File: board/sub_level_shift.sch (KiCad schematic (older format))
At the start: 24 parts, among them Q1401 Q_NPN_BEC, Q1402 Q_NPN_BEC, Q1403 Q_NPN_BEC, U1401 74LVC4245A, U1402 74LVC4245A, U1403 74LVC4245A, U1404 74LVC4245A, U1405 74LVC4245A, U1406 74LVC4245A, U1407 74LVC4245A

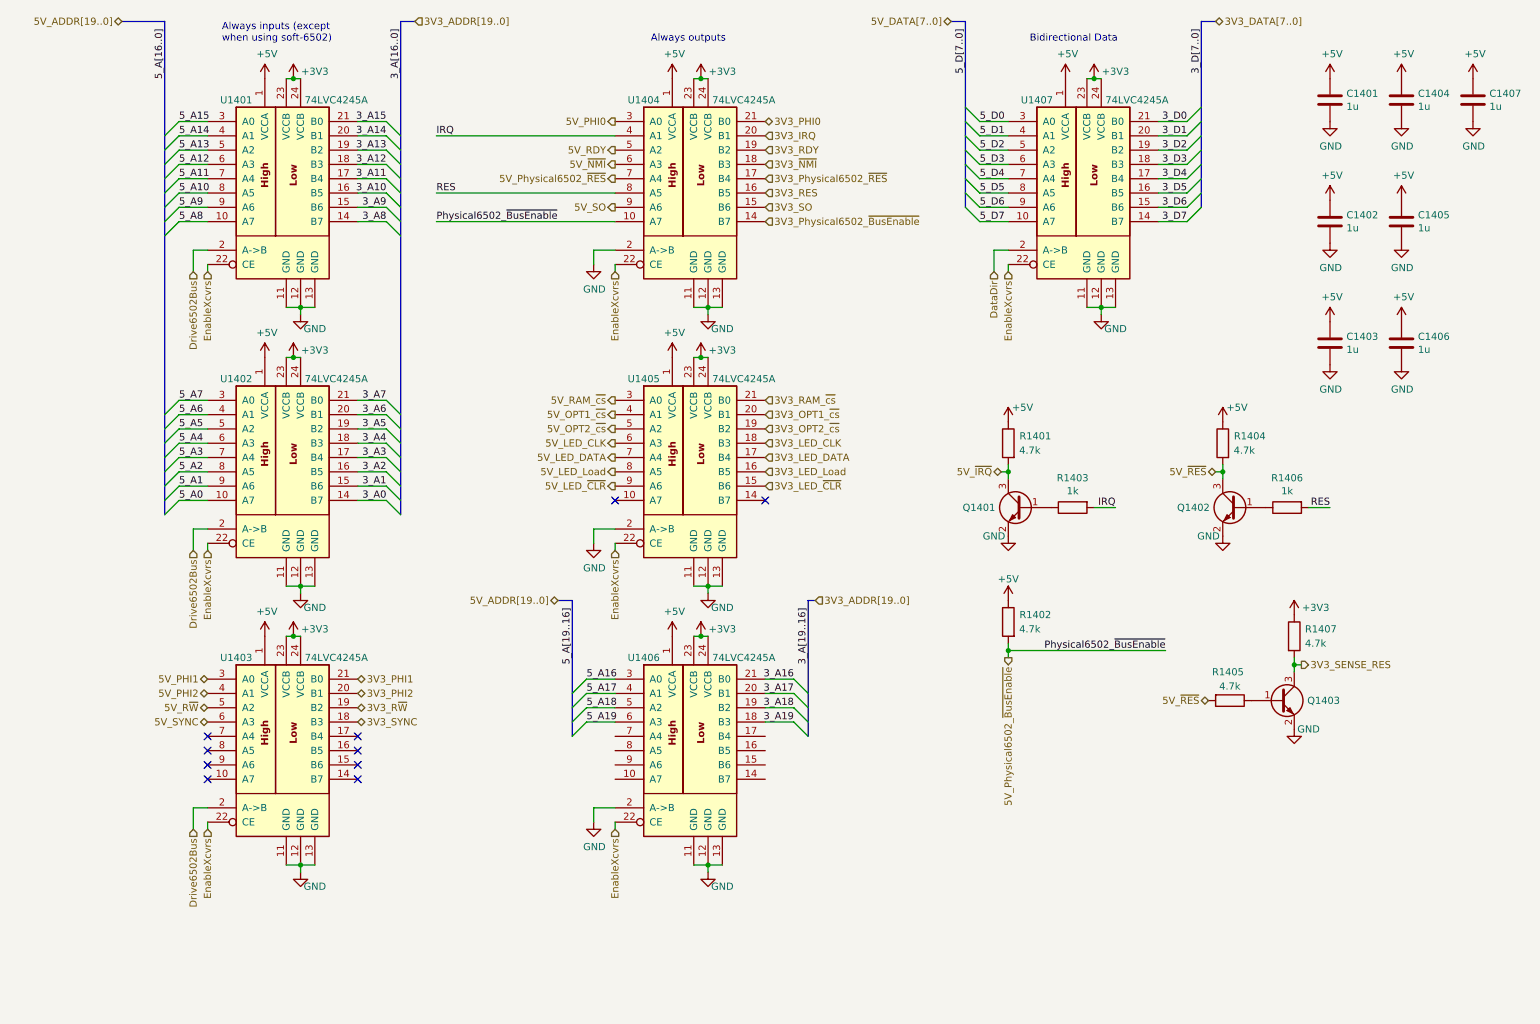
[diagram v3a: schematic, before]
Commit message: made some changes based on projected power budget
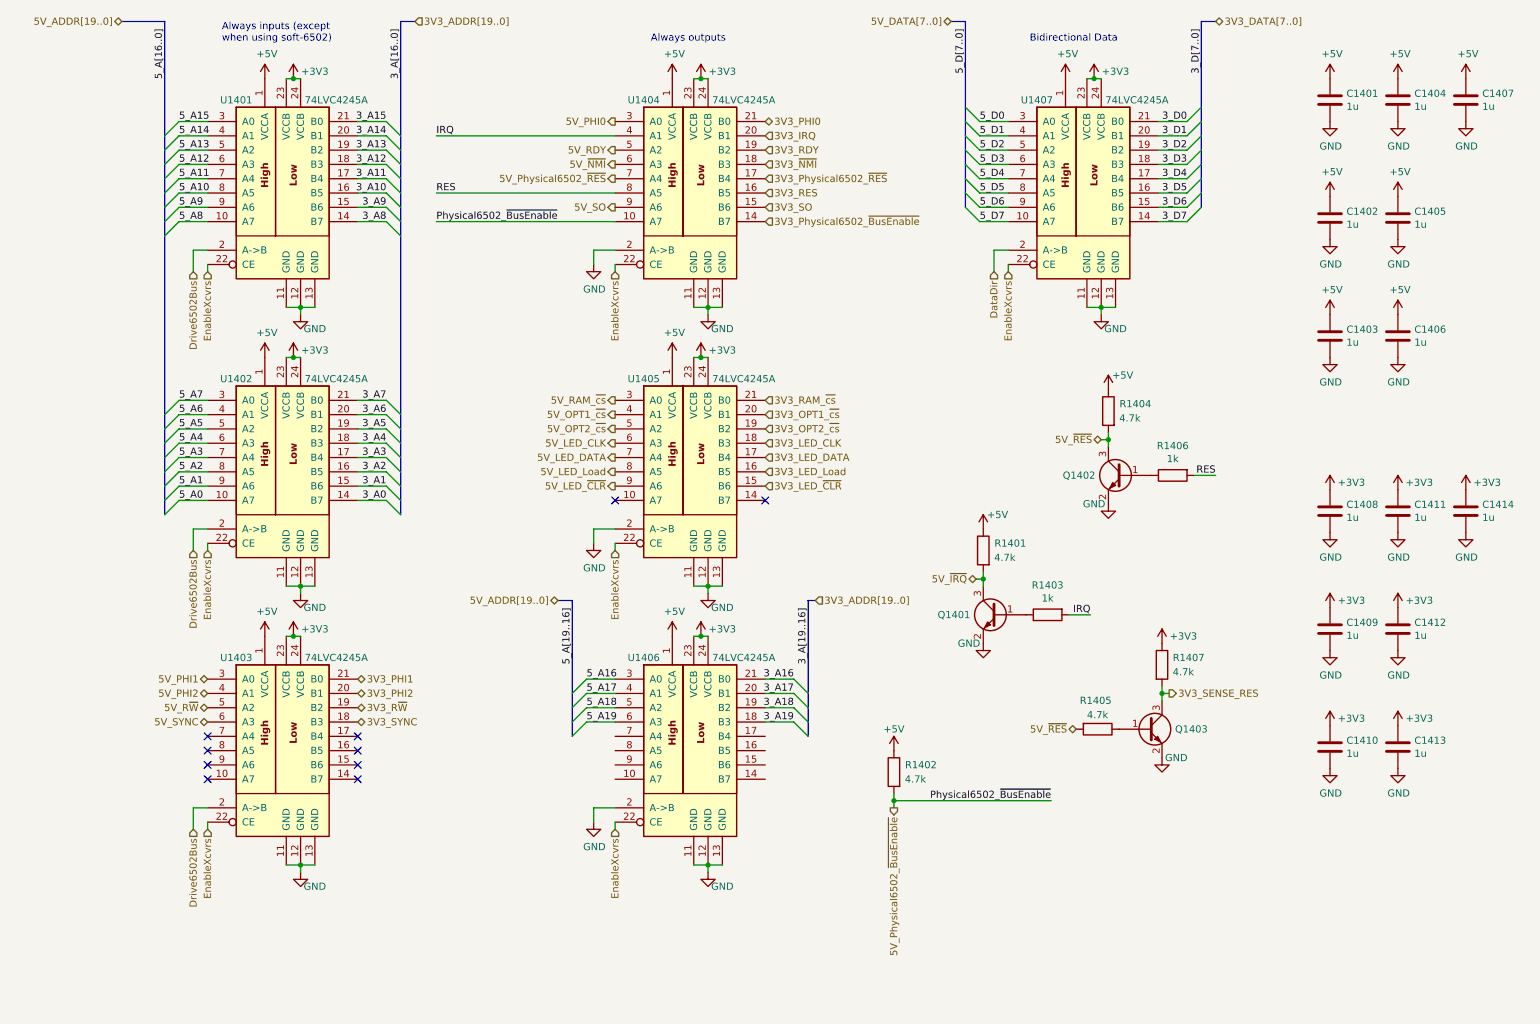
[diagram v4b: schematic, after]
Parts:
- added C1408, C1409, C1410, C1411, C1412, C1413, C1414: 1u, symbol Device:C
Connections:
- net +3V3: now also C1408.1, C1409.1, C1410.1, C1411.1, C1412.1, C1413.1, C1414.1
- net GND: now also C1408.2, C1409.2, C1410.2, C1411.2, C1412.2, C1413.2, C1414.2
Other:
- moved on the sheet: C1402, C1403, C1404, C1405, C1406, C1407, Q1401, Q1402, Q1403, R1401, R1402, R1403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

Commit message: Schematics mostly complete
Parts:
- renumbered C1404 to C1402, C1407 to C1403, C1402 to C1404, C1403 to C1406, C1406 to C1407, C1411 to C1409, C1414 to C1410, C1409 to C1411, C1410 to C1413, C1413 to C1414, Q1402 to Q1401, Q1401 to Q1402, R1404 to R1401, R1406 to R1402, R1401 to R1403, R1403 to R1404, R1407 to R1405, R1405 to R1406, R1402 to R1407, U1404 to U1402, U1407 to U1403, U1402 to U1404, U1403 to U1406, U1406 to U1407
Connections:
- net GND: now also U1407.14 (B7), U1407.15 (B6), U1407.16 (B5), U1407.17 (B4)
- net 3V3_LED_Load renamed 3V3_LED_LOAD
- net 5V_LED_Load renamed 5V_LED_LOAD
- no-connect marks 10 -> 14

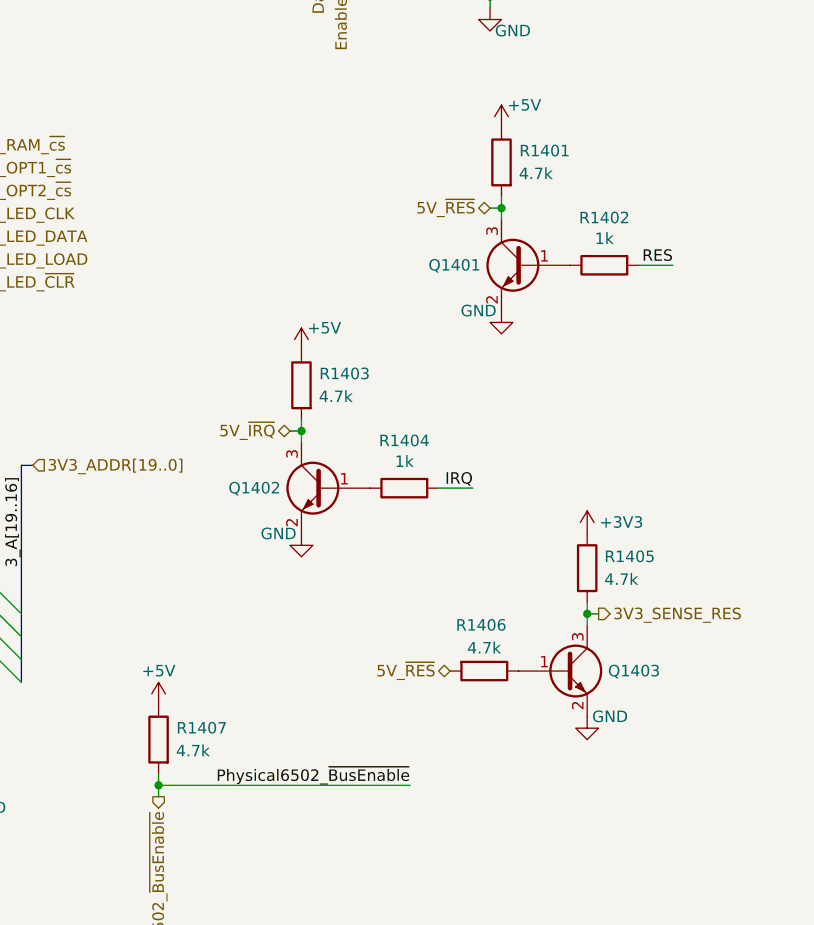
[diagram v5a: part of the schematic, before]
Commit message: Started picking footprints. Merged many components.
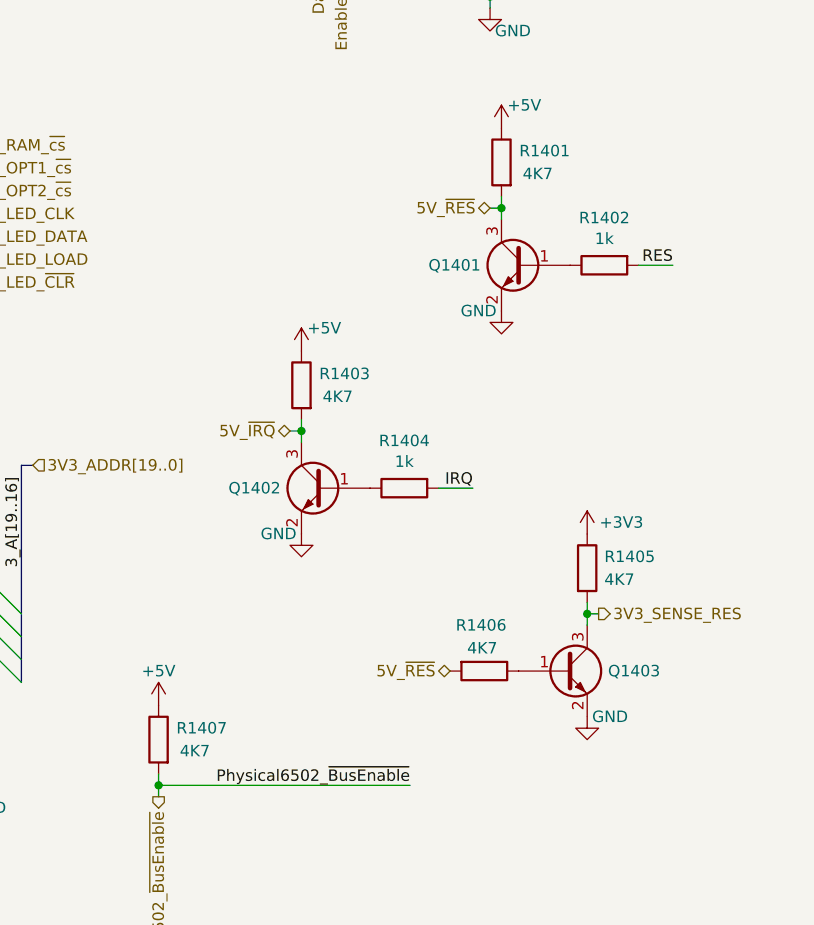
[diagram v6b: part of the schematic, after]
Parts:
- R1401, R1403, R1405, R1406, R1407: value 4.7k -> 4K7
- U1401, U1402, U1403, U1404, U1405, U1406, U1407: footprint (none) -> Package_SO:TSSOP-24_4.4x7.8mm_P0.65mm
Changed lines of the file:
@@
 $Descr A4 11693 8268
 encoding utf-8
-Sheet 14 14
+Sheet 14 15
 Title ""
 Date ""
@@
 F 0 "U1406" H 1950 6350 50  0000 C CNN
 F 1 "74LVC4245A" H 2650 6350 50  0000 C CNN
-F 2 "" H 2250 5700 50  0001 C CNN
+F 2 "Package_SO:TSSOP-24_4.4x7.8mm_P0.65mm" H 2250 5700 50  0001 C CNN
 F 3 "https://assets.nexperia.com/documents/data-sheet/74LVC4245A.pdf" H 2250 5700 50  0001 C CNN
 	1    2250 5700
@@
 F 0 "U1402" H 4800 2450 50  0000 C CNN
 F 1 "74LVC4245A" H 5500 2450 50  0000 C CNN
-F 2 "" H 5100 1800 50  0001 C CNN
+F 2 "Package_SO:TSSOP-24_4.4x7.8mm_P0.65mm" H 5100 1800 50  0001 C CNN
 F 3 "https://assets.nexperia.com/documents/data-sheet/74LVC4245A.pdf" H 5100 1800 50  0001 C CNN
 	1    5100 1800
@@
 F 0 "U1401" H 1950 2450 50  0000 C CNN
 F 1 "74LVC4245A" H 2650 2450 50  0000 C CNN
-F 2 "" H 2250 1800 50  0001 C CNN
+F 2 "Package_SO:TSSOP-24_4.4x7.8mm_P0.65mm" H 2250 1800 50  0001 C CNN
 F 3 "https://assets.nexperia.com/documents/data-sheet/74LVC4245A.pdf" H 2250 1800 50  0001 C CNN
 	1    2250 1800
@@
 F 0 "U1404" H 1950 4400 50  0000 C CNN
 F 1 "74LVC4245A" H 2650 4400 50  0000 C CNN
-F 2 "" H 2250 3750 50  0001 C CNN
+F 2 "Package_SO:TSSOP-24_4.4x7.8mm_P0.65mm" H 2250 3750 50  0001 C CNN
 F 3 "https://assets.nexperia.com/documents/data-sheet/74LVC4245A.pdf" H 2250 3750 50  0001 C CNN
 	1    2250 3750
@@
 F 0 "U1405" H 4800 4400 50  0000 C CNN
 F 1 "74LVC4245A" H 5500 4400 50  0000 C CNN
-F 2 "" H 5100 3750 50  0001 C CNN
+F 2 "Package_SO:TSSOP-24_4.4x7.8mm_P0.65mm" H 5100 3750 50  0001 C CNN
 F 3 "https://assets.nexperia.com/documents/data-sheet/74LVC4245A.pdf" H 5100 3750 50  0001 C CNN
 	1    5100 3750
@@
 P 7175 4300
 F 0 "R1403" H 6875 4350 50  0000 L CNN
-F 1 "4.7k" H 6950 4250 50  0000 L CNN
+F 1 "4K7" H 6950 4250 50  0000 L CNN
 F 2 "" V 7105 4300 50  0001 C CNN
 F 3 "~" H 7175 4300 50  0001 C CNN
@@
 P 6550 5850
 F 0 "R1407" H 6250 5900 50  0000 L CNN
-F 1 "4.7k" H 6325 5800 50  0000 L CNN
+F 1 "4K7" H 6325 5800 50  0000 L CNN
 F 2 "" V 6480 5850 50  0001 C CNN
 F 3 "~" H 6550 5850 50  0001 C CNN
@@
 F 0 "U1403" H 7550 2450 50  0000 C CNN
 F 1 "74LVC4245A" H 8250 2450 50  0000 C CNN
-F 2 "" H 7850 1800 50  0001 C CNN
+F 2 "Package_SO:TSSOP-24_4.4x7.8mm_P0.65mm" H 7850 1800 50  0001 C CNN
 F 3 "https://assets.nexperia.com/documents/data-sheet/74LVC4245A.pdf" H 7850 1800 50  0001 C CNN
 	1    7850 1800
@@
 F 0 "U1407" H 4800 6350 50  0000 C CNN
 F 1 "74LVC4245A" H 5500 6350 50  0000 C CNN
-F 2 "" H 5100 5700 50  0001 C CNN
+F 2 "Package_SO:TSSOP-24_4.4x7.8mm_P0.65mm" H 5100 5700 50  0001 C CNN
 F 3 "https://assets.nexperia.com/documents/data-sheet/74LVC4245A.pdf" H 5100 5700 50  0001 C CNN
 	1    5100 5700
@@
 P 8050 3325
 F 0 "R1401" H 7750 3375 50  0000 L CNN
-F 1 "4.7k" H 7825 3275 50  0000 L CNN
+F 1 "4K7" H 7825 3275 50  0000 L CNN
 F 2 "" V 7980 3325 50  0001 C CNN
 F 3 "~" H 8050 3325 50  0001 C CNN
@@
 P 8425 5100
 F 0 "R1405" H 8500 5150 50  0000 L CNN
-F 1 "4.7k" H 8500 5050 50  0000 L CNN
+F 1 "4K7" H 8500 5050 50  0000 L CNN
 F 2 "" V 8355 5100 50  0001 C CNN
 F 3 "~" H 8425 5100 50  0001 C CNN
@@
 P 7975 5550
 F 0 "R1406" V 7775 5425 50  0000 L CNN
-F 1 "4.7k" V 7875 5475 50  0000 L CNN
+F 1 "4K7" V 7875 5475 50  0000 L CNN
 F 2 "" V 7905 5550 50  0001 C CNN
 F 3 "~" H 7975 5550 50  0001 C CNN
@@
 Wire Wire Line
 	5650 5900 5800 5900
+Connection ~ 5800 5900
+Wire Wire Line
+	5800 5900 5800 5975
 Wire Bus Line
 	5950 4650 5950 5600
@@
 Wire Bus Line
 	1450 600  1450 4050
-Connection ~ 5800 5900
-Wire Wire Line
-	5800 5900 5800 5975
 $EndSCHEMATC

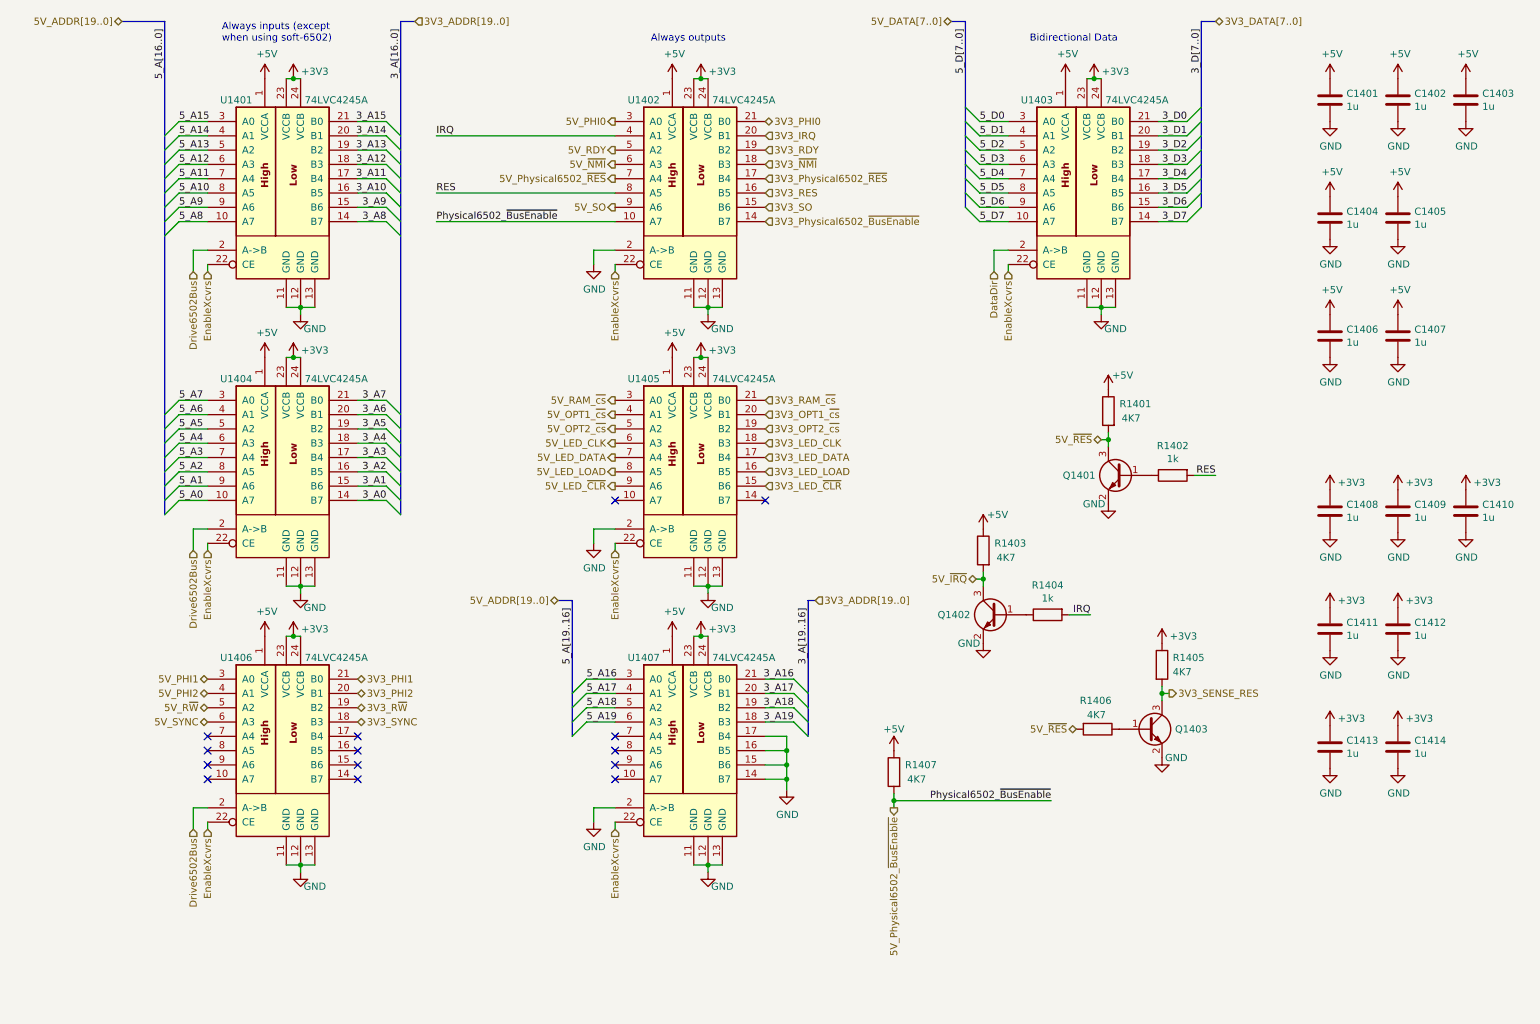
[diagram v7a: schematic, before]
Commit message: Fixed swapped pin and some labels
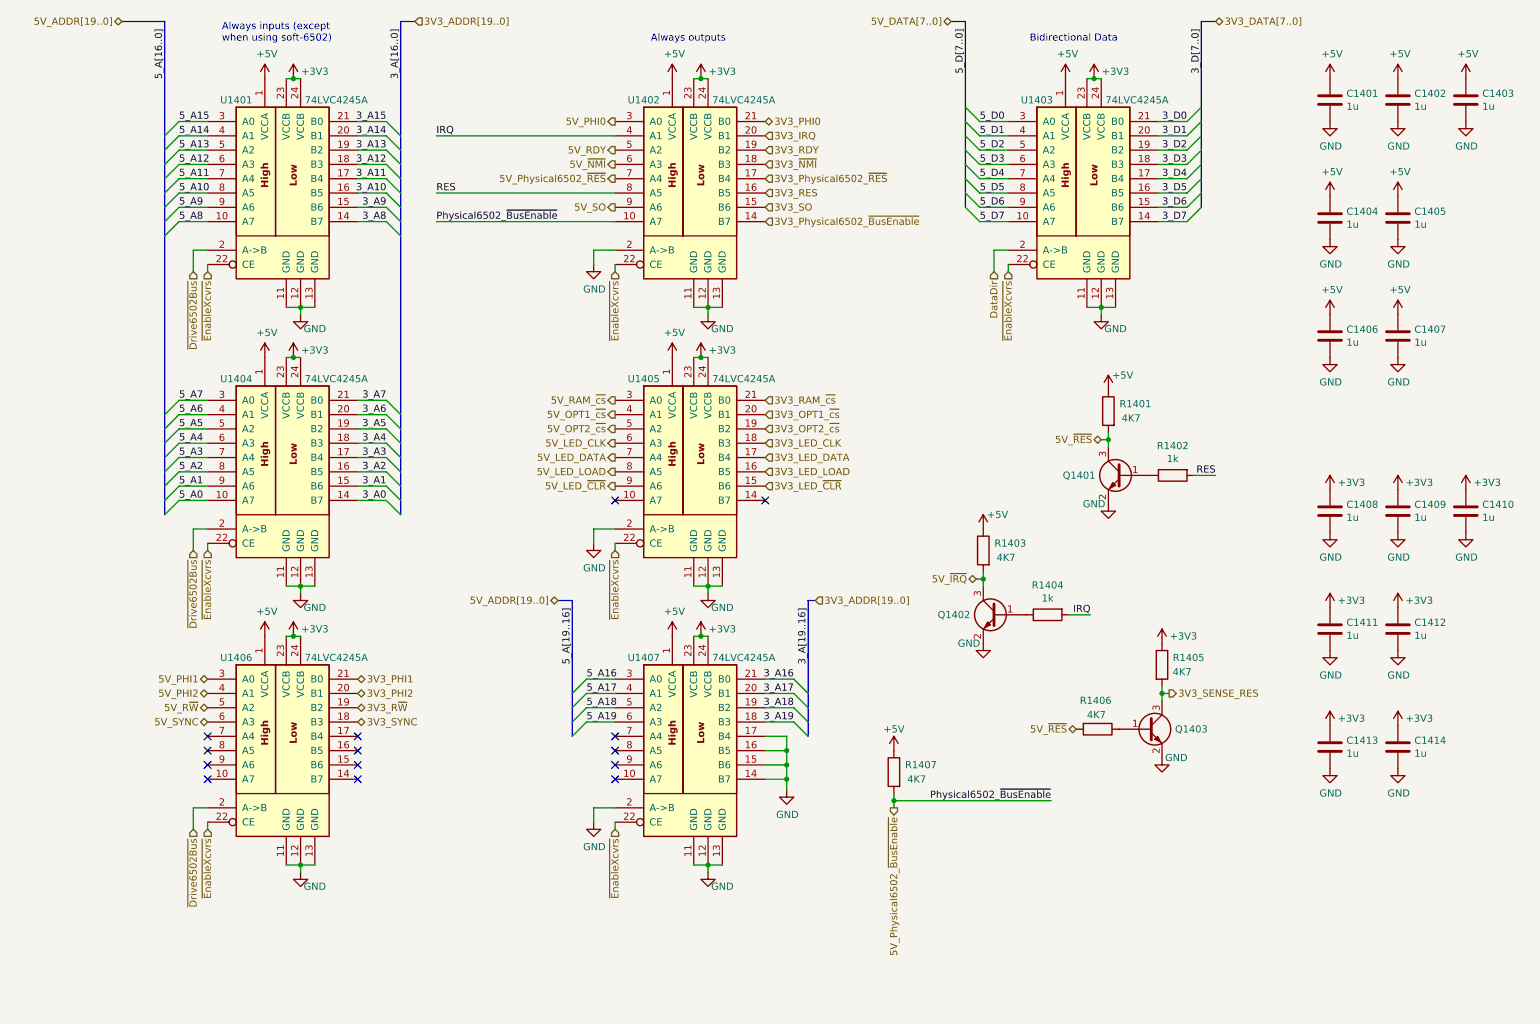
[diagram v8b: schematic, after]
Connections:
- net Drive6502Bus renamed ~Drive6502Bus
- net EnableXcvrs renamed ~EnableXcvrs
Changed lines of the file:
@@
 Wire Wire Line
 	5350 6500 5250 6500
-Text HLabel 4600 2350 3    50   Input ~ 0
-EnableXcvrs
-Text HLabel 4600 4300 3    50   Input ~ 0
-EnableXcvrs
-Text HLabel 4600 6250 3    50   Input ~ 0
-EnableXcvrs
-Text HLabel 1750 6250 3    50   Input ~ 0
-EnableXcvrs
-Text HLabel 1750 4300 3    50   Input ~ 0
-EnableXcvrs
 Text HLabel 1750 2350 3    50   Input ~ 0
-EnableXcvrs
-Text HLabel 7350 2350 3    50   Input ~ 0
-EnableXcvrs
+~EnableXcvrs
 Wire Wire Line
 	7350 2350 7350 2300
@@
 	1750 6250 1750 6200
 Text HLabel 1650 2350 3    50   Input ~ 0
-Drive6502Bus
+~Drive6502Bus
 Text HLabel 1650 4300 3    50   Input ~ 0
-Drive6502Bus
+~Drive6502Bus
 Text HLabel 1650 6250 3    50   Input ~ 0
-Drive6502Bus
+~Drive6502Bus
 Wire Wire Line
 	1650 2350 1650 2200
@@
 Wire Bus Line
 	1450 600  1450 4050
+Text HLabel 7350 2350 3    50   Input ~ 0
+~EnableXcvrs
+Text HLabel 1750 4300 3    50   Input ~ 0
+~EnableXcvrs
+Text HLabel 1750 6250 3    50   Input ~ 0
+~EnableXcvrs
+Text HLabel 4600 6250 3    50   Input ~ 0
+~EnableXcvrs
+Text HLabel 4600 4300 3    50   Input ~ 0
+~EnableXcvrs
+Text HLabel 4600 2350 3    50   Input ~ 0
+~EnableXcvrs
 $EndSCHEMATC
